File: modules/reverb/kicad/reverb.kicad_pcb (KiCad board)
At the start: 2 copper layers, 69 parts, among them P1 CONN_01X02, P2 CONN_01X03, P3 CONN_01X02, P4 CONN_01X03, P5 CONN_01X03, P6 CONN_01X02, P7 CONN_01X02, P8 CONN_01X02, P9 CONN_01X02, Q1 2N3906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

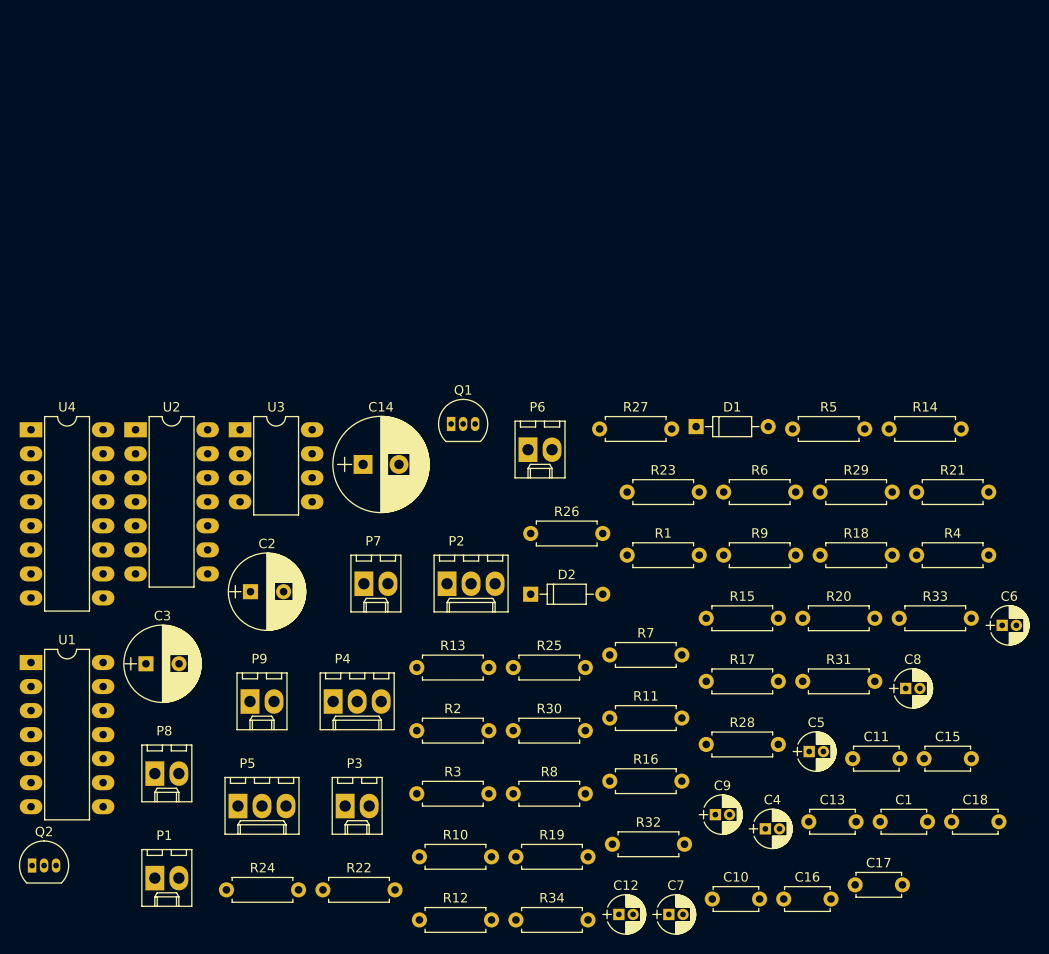
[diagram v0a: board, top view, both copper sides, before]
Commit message: Lay out reverb PCB
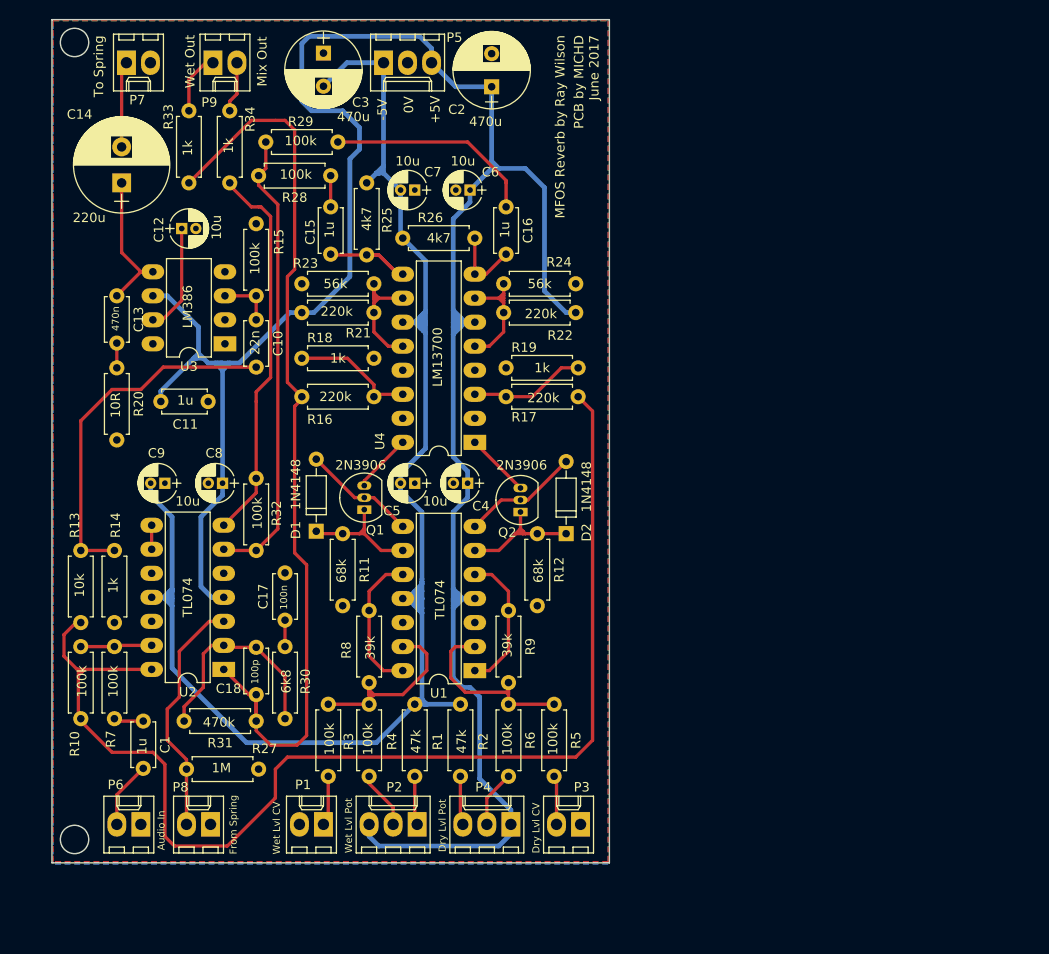
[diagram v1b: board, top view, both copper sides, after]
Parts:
- C18: value 100n -> 100p
- moved C13 91.9 mm to (122.8, 75.1), turned to 270 degrees
- moved R33 88.1 mm to (130.4, 63.1), turned to 90 degrees
- moved C12 86.0 mm to (129.7, 67.9)
- moved C15 85.7 mm to (145.4, 65.7), turned to 270 degrees
- moved R14 84.4 mm to (122.6, 109.6), turned to 90 degrees
- moved R34 83.6 mm to (134.7, 63.1), turned to 90 degrees
- moved C7 81.1 mm to (154.3, 63.9), turned to 180 degrees
- moved P5 80.1 mm to (151.0, 50.4)
- moved C16 78.8 mm to (164.0, 65.7), turned to 270 degrees
- moved C1 78.6 mm to (125.6, 120.0), turned to 270 degrees
- moved C10 77.9 mm to (137.5, 77.6), turned to 270 degrees
- moved C11 77.9 mm to (132.5, 86.2), turned to 180 degrees
- moved R20 77.2 mm to (122.8, 82.7), turned to 270 degrees
- moved C8 75.4 mm to (134.0, 94.9), turned to 180 degrees
- moved C18 74.7 mm to (137.5, 117.2), turned to 90 degrees
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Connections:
- P1 pad 1: GND -> Net-(P1-Pad1)
- P1 pad 2: Net-(P1-Pad2) -> GND
- P4 pad 1: Net-(P4-Pad1) -> VCC
- P4 pad 3: VCC -> Net-(P4-Pad3)
- R2 pad 1: Net-(P4-Pad1) -> Net-(P4-Pad3)
- R3 pad 2: Net-(P1-Pad2) -> Net-(P1-Pad1)
- U1 pad 1: Net-(R8-Pad1) -> Net-(R9-Pad1)
- U1 pad 10: GND -> Net-(R8-Pad1)
- U1 pad 12: Net-(R9-Pad1) -> GND
- U1 pad 13: Net-(D2-Pad1) -> Net-(R3-Pad1)
- U1 pad 14: Net-(D2-Pad2) -> Net-(R8-Pad1)
- U1 pad 2: Net-(R3-Pad1) -> Net-(R5-Pad1)
- U1 pad 5: Net-(R8-Pad1) -> Net-(R9-Pad1)
- U1 pad 6: Net-(D1-Pad1) -> Net-(D2-Pad1)
- U1 pad 7: Net-(D1-Pad2) -> Net-(D2-Pad2)
- U1 pad 8: Net-(R9-Pad1) -> Net-(D1-Pad2)
- U1 pad 9: Net-(R5-Pad1) -> Net-(D1-Pad1)
- U2 pad 1: DRY-SIGNAL -> WET-SIGNAL
- U2 pad 13: Net-(U2-Pad13) -> Net-(R10-Pad2)
- U2 pad 14: Net-(U2-Pad13) -> DRY-SIGNAL
- U2 pad 2: Net-(R10-Pad2) -> Net-(C18-Pad2)
- U2 pad 3: GND -> Net-(P8-Pad2)
- U2 pad 5: Net-(P8-Pad2) -> GND
- U2 pad 6: Net-(C18-Pad2) -> Net-(R28-Pad2)
- U2 pad 7: WET-SIGNAL -> Net-(R32-Pad2)
- U2 pad 8: Net-(R32-Pad2) -> Net-(U2-Pad8)
- U2 pad 9: Net-(R28-Pad2) -> Net-(U2-Pad8)
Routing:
- net VCC: track 0.00 -> 263.5 mm
- net VEE: track 0.00 -> 170.8 mm
- net DRY-SIGNAL: track 0.00 -> 128.6 mm
- net WET-SIGNAL: track 0.00 -> 97.8 mm
- net Net-(R28-Pad2): track 0.00 -> 48.8 mm
- net Net-(R32-Pad2): track 0.00 -> 40.6 mm
- net Net-(C10-Pad2): track 0.00 -> 38.2 mm
- net Net-(P8-Pad2): track 0.00 -> 25.9 mm
- net Net-(C18-Pad2): track 0.00 -> 22.8 mm
- net Net-(C16-Pad1): track 0.00 -> 22.3 mm
- net Net-(R5-Pad1): track 0.00 -> 20.8 mm
- net Net-(R3-Pad1): track 0.00 -> 20.6 mm
- net Net-(R8-Pad1): track 0.00 -> 15.3 mm
- net Net-(C13-Pad1): track 0.00 -> 15.1 mm
- net Net-(R9-Pad1): track 0.00 -> 15.0 mm
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- added copper zone on B.Cu, net GND
- added copper zone on F.Cu, net GND
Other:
- board outline added: 58.9 x 89.1 mm
- net class Default: clearance 0.2 -> 0.25; trace_width 0.25 -> 0.35
- net class Power added: clearance 0.25, trace_width 0.5, via_dia 0.6, via_drill 0.4
- rule trace_clearance: 0.2 -> 0.25
- board text added: "+5V"
- board text added: "-5V"
- board text added: "0V"
- board text added: "Audio In"
- board text added: "Dry Lvl CV"
- board text added: "Dry Lvl Pot"
- board text added: "From Spring"
- board text added: "MFOS Reverb by Ray Wilson"
- board text added: "Mix Out"
- board text added: "PCB by MICHD June 2017"
- board text added: "To Spring"
- board text added: "Wet Lvl CV"
- board text added: "Wet Lvl Pot"
- board text added: "Wet Out"

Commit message: Correct some component values on reverb schematic/pcb
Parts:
- C13: value 470n -> 47n
- R11, R12: value 68k -> 6k8
- R32: value 100k -> 150k
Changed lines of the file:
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@@
       (effects (font (size 1 1) (thickness 0.15)))
     )
-    (fp_text value 470n (at 2.413 0.127 270) (layer F.SilkS)
+    (fp_text value 47n (at 2.413 0.127 270) (layer F.SilkS)
       (effects (font (size 0.75 0.75) (thickness 0.125)))
     )
@@
       (effects (font (size 1 1) (thickness 0.15)))
     )
-    (fp_text value 68k (at 3.937 0.127 270) (layer F.SilkS)
+    (fp_text value 6k8 (at 3.937 0.127 270) (layer F.SilkS)
       (effects (font (size 1 1) (thickness 0.15)))
     )
@@
       (effects (font (size 1 1) (thickness 0.15)))
     )
-    (fp_text value 68k (at 3.937 -0.127 270) (layer F.SilkS)
+    (fp_text value 6k8 (at 3.937 -0.127 270) (layer F.SilkS)
       (effects (font (size 1 1) (thickness 0.15)))
     )
@@
       (effects (font (size 1 1) (thickness 0.15)))
     )
-    (fp_text value 100k (at 3.937 0.127 90) (layer F.SilkS)
-      (effects (font (size 1 1) (thickness 0.15)))
-    )
+    (fp_text value 150k (at 3.937 0.127 90) (layer F.SilkS)
+      (effects (font (size 1 1) (thickness 0.15)))
+    )
